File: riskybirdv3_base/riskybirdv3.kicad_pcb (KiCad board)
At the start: 4 copper layers, 70 x 70.6 mm, 181 parts, among them IC1 PMW3901MB-TXQT, J1 Conn_02x10_Odd_Even, J10 Conn_01x05, J11 Conn_01x05, J2 Conn_01x05, J3 Conn_01x02, J4 Conn_01x02, J5 Conn_01x02, J6 Conn_01x02, J8 USB_C_Receptacle_USB2.0_16P, J9 Conn_01x05, Q1 SI2302, Q2 SI2302, Q3 SI2302, Q4 SI2302, Q5 AON7407, Q6 2N7002, Q7 2N7002, Q9 AON7534, SW1 SW_SPST, SW2 SW_SPST, SW4 SW_SPST, SW5 SW_SPST, U1 ADS7128IRTER, U10 TLV70018DCKR, U11 TLV70015DCKT, U12 PCA9306DC, U13 LM74700, U14 ESP32-C6-MINI-1/U, U2 LTC3119EUFD#TRPBF, U3 BMI088, U4 MCP73831-2-OT, U6 USBLC6-2P6, U7 TLV70028DCKR, U8 LM66100DCK, U9 VL53L1CXV0FY1

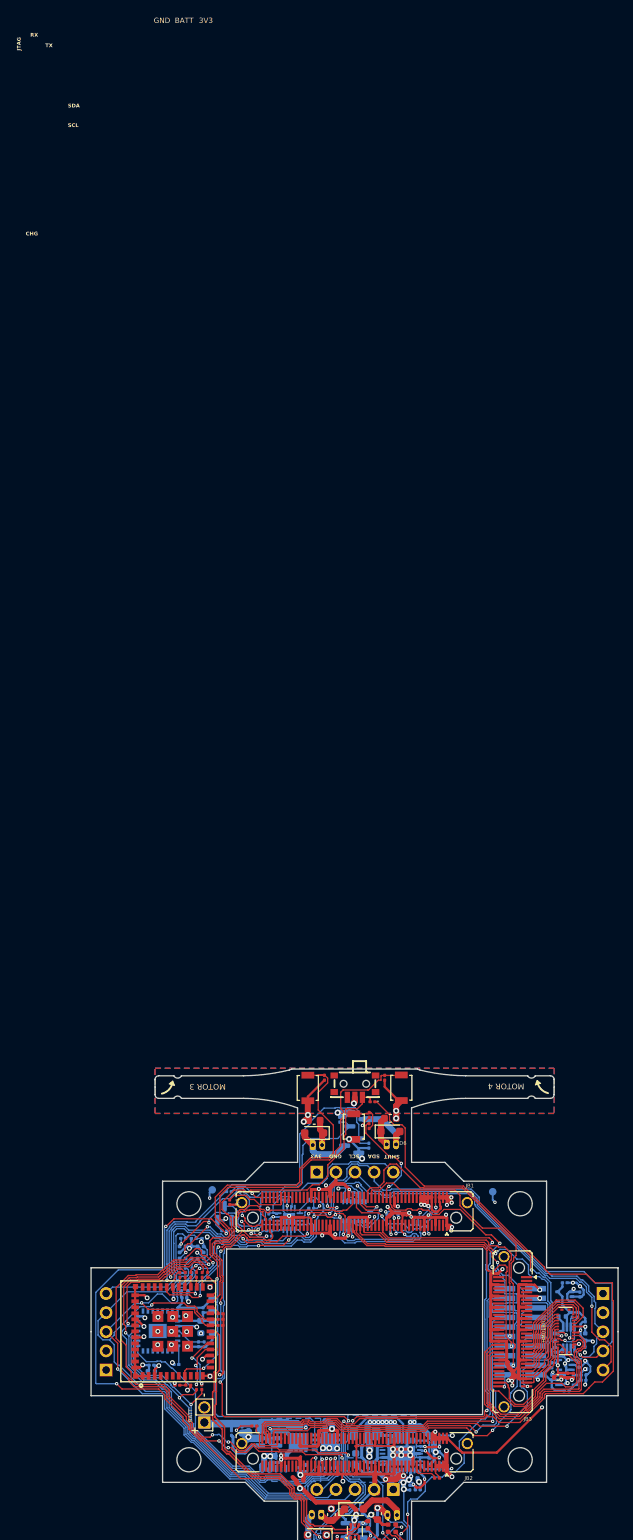
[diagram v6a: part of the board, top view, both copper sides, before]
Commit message: riskybirdv3: JLC part-matching + camera connector fix (checkpoint before FPGA rework)
- Assign LCSC/MPN to unmatched parts for JLC assembly: J1 FTSH-110, J3-6 PicoBlade, J8 USB-C, R71, SW1/2/4, SW5, U4 MCP73831, U5 BMP390L, U14 ESP32-C6-MINI-1U
- B2B JB1/JB2/JB3 -> Samtec LSHM-1x0-04.0 (8mm stack, in-stock): C5367357/C3645597
- Camera HM01B0: plug 503776-2410 -> receptacle 505550-2420 (C3642262); import Molex receptacle footprint, renumber pads to ring numbering (pin1 top-right CW) per physical part, fix attr smd
- PCB silkscreen fixes + in-progress routing
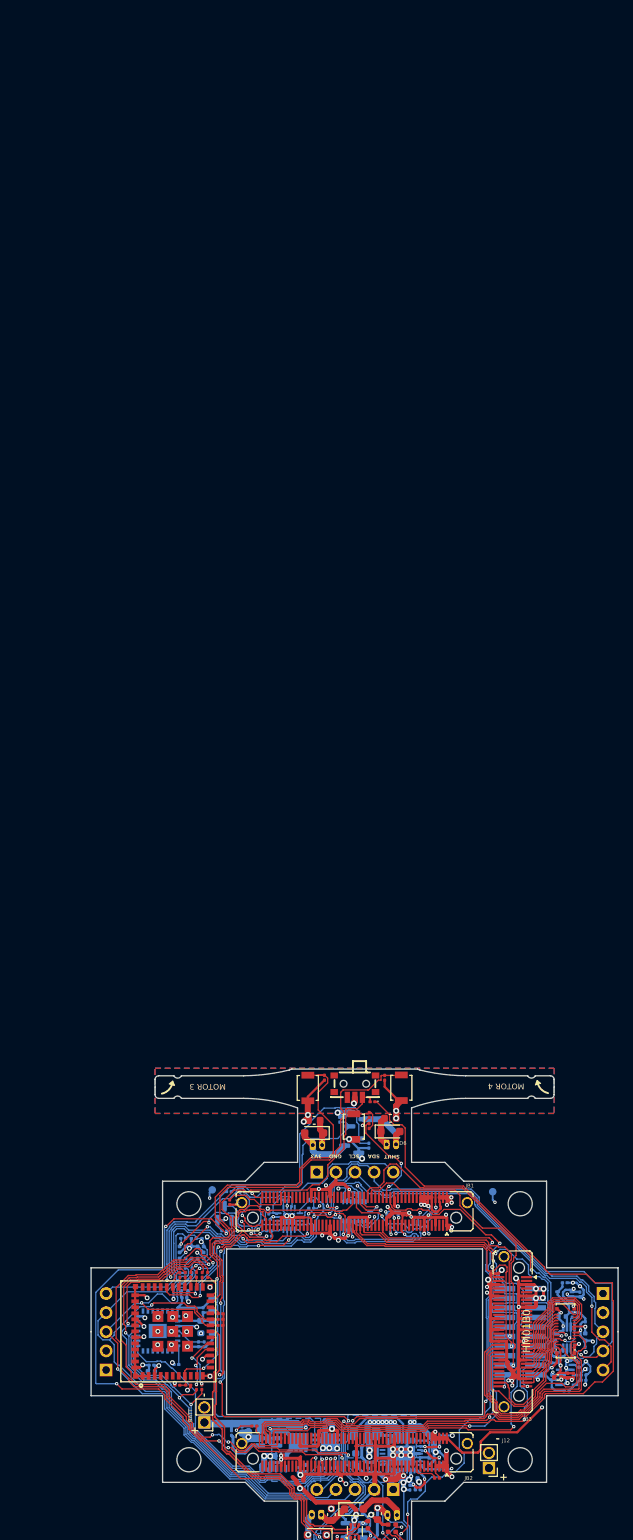
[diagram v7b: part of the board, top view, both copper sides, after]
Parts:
- added J12: Conn_01x02, Connector_PinHeader_2.00mm:PinHeader_1x02_P2.00mm_Vertical, F.Cu at (117.8, 118.1)
- HM01B0: footprint riskybird:5037762410 -> riskybird_lcsc:CONN-SMD_24P-P0.40_5055502420
- U5: value ~ -> BMP390
- moved G1 22.5 mm to (118.2, 113.3), turned to 180 degrees
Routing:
- net GND: track 487.3 -> 530.6 mm, vias 93 -> 112
- net /FPGA_TDI: track 48.9 -> 47.5 mm
- net /FVLD: track 32.0 -> 30.6 mm
- net /D4: track 12.9 -> 14.1 mm
- net Net-(JB1-Pin_32): track 68.9 -> 70.1 mm
- net /D2: track 13.7 -> 14.8 mm
- net /FPGA_TMS: track 50.1 -> 51.0 mm
- net +3V3: track 153.8 -> 154.7 mm
- net /FPGA_TDO: track 53.2 -> 53.9 mm
- net /FPGA_TCK: track 50.9 -> 50.3 mm
- net /D0: track 14.9 -> 15.5 mm
- net +1V8: track 92.8 -> 93.4 mm
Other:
- board text removed: "BATT"
- board text removed: "CHG"
- board text removed: "JTAG"
- board text removed: "RX"
- board text removed: "TX"
